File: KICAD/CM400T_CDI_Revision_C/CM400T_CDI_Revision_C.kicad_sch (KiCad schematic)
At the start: 41 parts, among them P1 Brown, P2 Green Coil, P3 Black w/ White, P4 Yellow Coil, P5 Blue, P6 White, P7 Light Blue, P8 Green Harness, P9 Pink

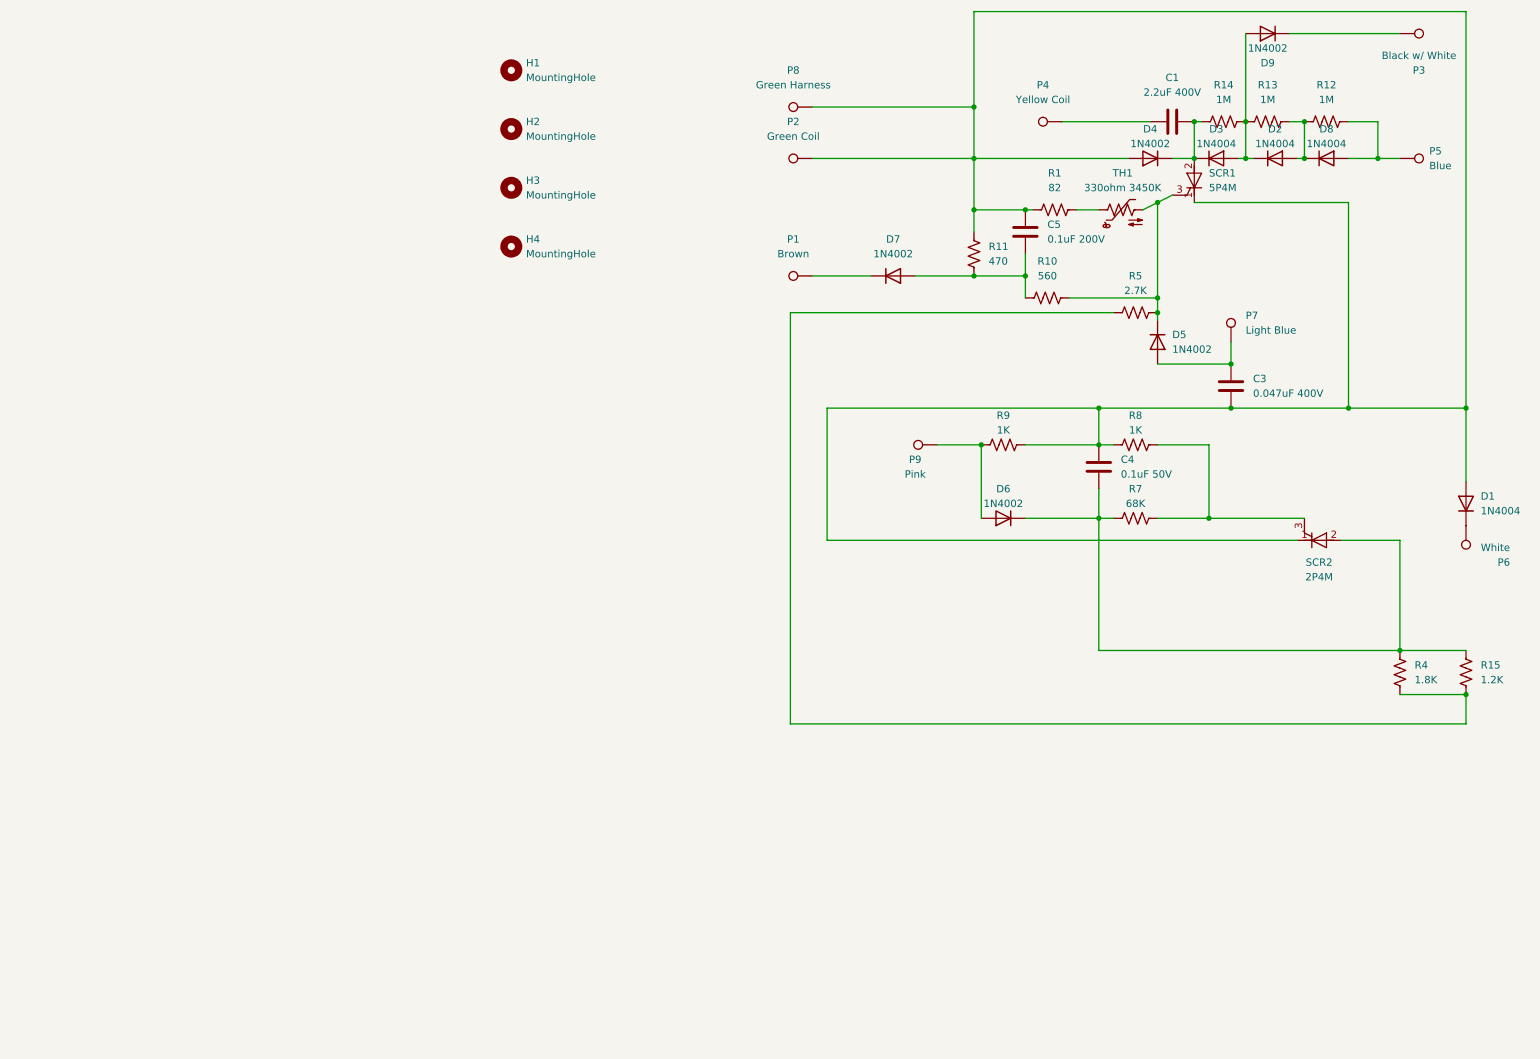
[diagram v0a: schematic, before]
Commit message: Redraw schematic to match structure of diagram from manual. No electrical / functional changes
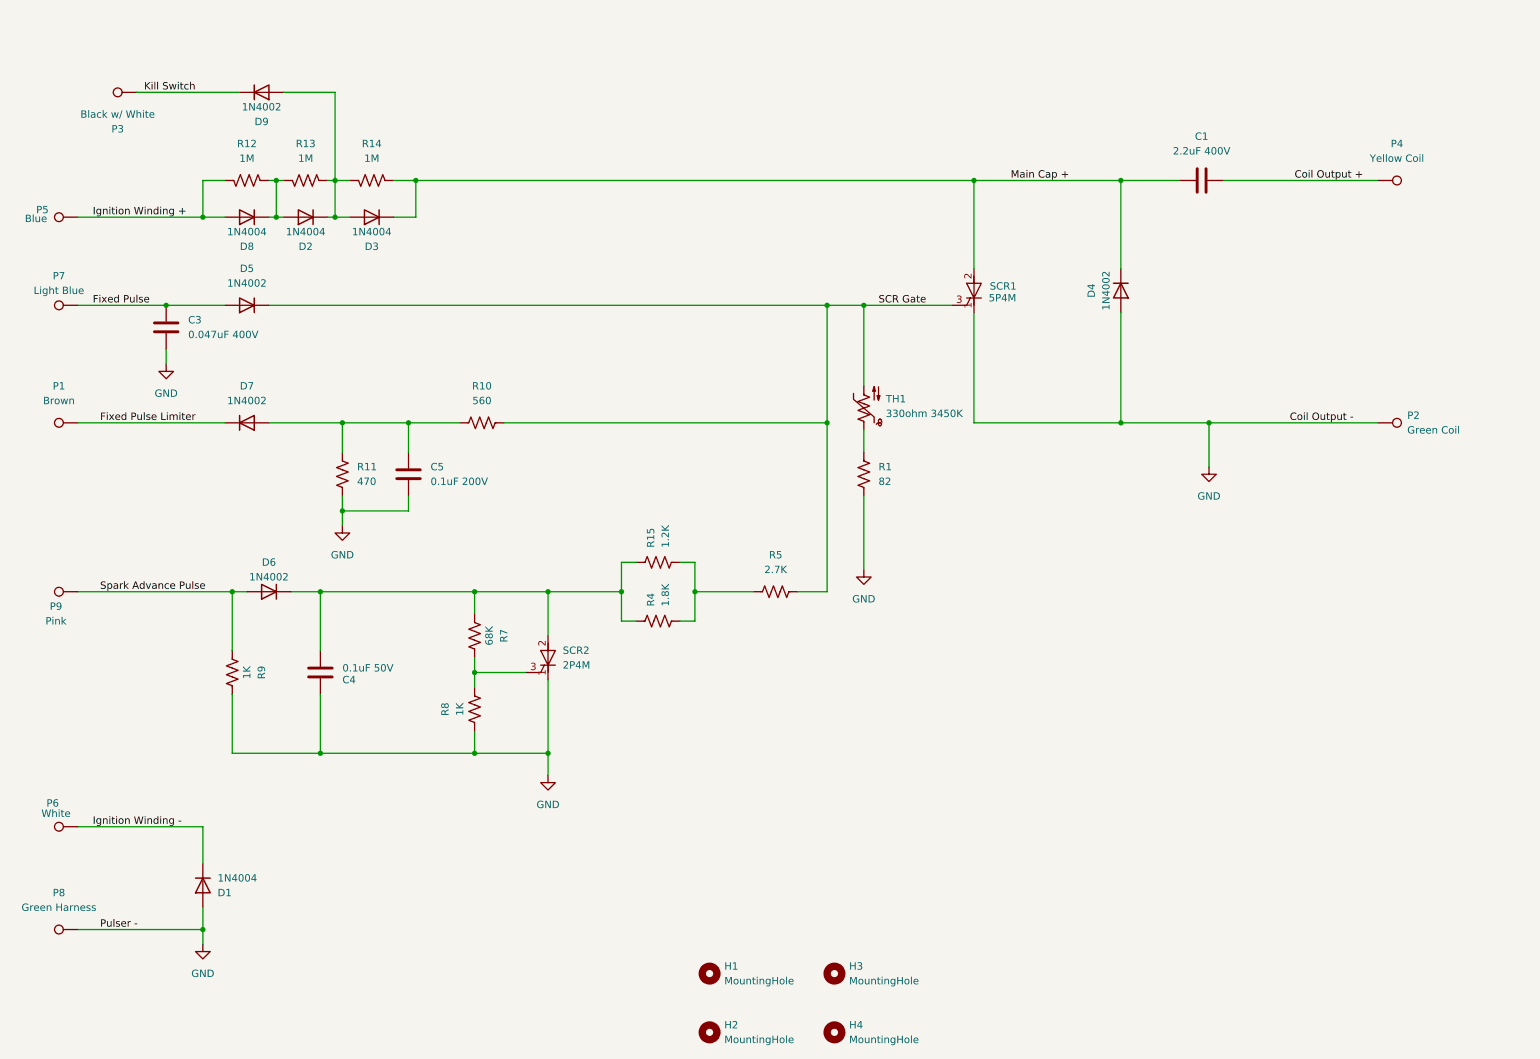
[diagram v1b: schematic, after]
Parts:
- C5: footprint Capacitor_THT:C_Axial_L3.8mm_D2.6mm_P12.50mm_Horizontal -> Capacitor_THT:C_Axial_L3.8mm_D2.6mm_P15.00mm_Horizontal
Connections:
- net Ignition Winding -: now reaches D1.1 (K), P6.1
- net GND: now reaches C3.2, C4.1, C5.2, D1.2 (A), D4.2 (A), P2.1, P8.1, R1.1, R11.1, R8.1, R9.2, SCR1.1 (K), SCR2.1 (K)
- net Main Cap +: now reaches C1.2, D3.1 (K), D4.1 (K), R14.1, SCR1.2 (A)
- net SCR Gate: now reaches D5.1 (K), R10.2, R5.2, SCR1.3 (G), TH1.2
- net Spark Advance Pulse: now reaches D6.2 (A), P9.1, R9.1
- net Fixed Pulse Limiter: now reaches D7.1 (K), P1.1
- net Coil Output +: now reaches C1.1, P4.1
- net Kill Switch: now reaches D9.1 (K), P3.1
- net Fixed Pulse: now reaches C3.1, D5.2 (A), P7.1
- net Ignition Winding +: now reaches D8.2 (A), P5.1, R12.1
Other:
- moved on the sheet: C1, C3, C4, C5, D1, D2, D3, D4, D5, D6, D7, D8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

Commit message: Add footprint file for 35mm capacitor to fix DRC violation
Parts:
- C1: footprint Capacitor_THT:C_Axial_L3.8mm_D2.6mm_P12.50mm_Horizontal -> footprints:C_Axial_L3.8mm_D2.6mm_P35.00mm_Horizontal
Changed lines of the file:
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@@
 			"3uvSlIUPRIG014WlBCxqh1z0imRm11nh1nI2SGSCdQ2FLKw0/CuDuYJWLdAgpF6PSaZSqStloVWV"
 			"M7FAfSczx+ysk+zxUmLAQs6Iv7J7K4HwlmyzErp9aQEjRO54VgIIVo4SWFD0wE6Lps9adrcBpIG7"
-			"iw3DcLlckOb/A3P5Xpd7T4mZAAAAAElFTkSuQmCC"
+			"iw3DcLlckOb/A3P5Xpd7T4mZAAAAAElFTkSuQmCCeIx0cAd7CAd5SIdwcAd6cAN2eIdwIIcZzBEO"
+			"7JAO4TAPbjAP4/AO8FAOMxDEHd4hHNghHcJhHmYwiTu8gzvQQzm0Azy8gzyEAzvM8BR2YAd7aAc3"
+			"aIdyaAc3gIdwkIdwYAd2KAd2+AV2eId3gIdfCIdxGIdymId5mIEs7vAO7uAO9cAO7DADYsihHOSh"
+			"HMyhHOShHNxhHMohHMSBHcphBtaQQznIQzmYQznIQzm4wziUQziIAzuUwy+8gzz8gjvUAzuwwwzH"
+			"aYdwWIdycIN0aAd4YId0GId0oIcZzlMP7gAP8lAO5JAO40AP4SAO7FAOMyAoHdzBHsJBHtIhHNyB"
+			"HtzgHOThHeoBHmYYUTiwQzqcgzvMUCR2YAd7aAc3YId3eAd4mFFM9JAP8FAOMx5qHsphHOghHd7B"
+			"HX4BHuShHMwhHfBhBlSFgzjMwzuwQz3QQzn8wjzkQzuIwzuww4zFCod5mId3GId0CAd6KAdymIFc"
+			"4xAO7MAO5VAO8zAjwdJBHuThF9jhHd4BHgAAAAB5IAAADQMAAGIeSCBDiAwZORkkkJFAxsjIaCJQ"
+			"CBQynhgZIUfIkFGkB16wQwEAAABNhCSHcylJE12X8zgP96gBx02ShnFKR1lTdRlIhGFalxhLdBUG"
+			"sTzXdVHTZVyG1WjR0ijSAlWPASGagylGJEEb1iwM8mAYRUmSJEULUU1fGFiZshwX9kCcBAAAAGZ1"
+			"bmN0aW9uX3R5cGVpbXBsaWNpdF9hcmdfZGVzY01vZHVsZU1EaXNQcmVjaXNlY29tcE9wdERlbm9y"
+			"bXNBcmVaZXJvQ29ycmVjdGx5Um91bmRlZERpdlNxcnRPcHREaXNhYmxlTWFkRW5hYmxlTm9TaWdu"
+			"ZWRaZXJvc0Zsb2F0Um91bmRpbmdNb2RlRmxvYXRDdnRJbnRSb3VuZGluZ01vZGVVbnNhZmVNYXRo"
+			"T3B0aW1pemF0aW9uc0Zpbml0ZU1hdGhPbmx5RmFzdFJlbGF4ZWRNYXRoRGFzaEdTcGVjaWZpZWRG"
+			"YXN0Q29tcGlsYXRpb25Vc2VTY3JhdGNoU3BhY2VQcml2YXRlTWVtb3J5UmVsYXhlZEJ1aWx0aW5z"
+			"U3ViZ3JvdXBJbmRlcGVuZGVudEZvcndhcmRQcm9ncmVzc1JlcXVpcmVkR3JlYXRlclRoYW4yR0JC"
+			"dWZmZXJSZXF1aXJlZEdyZWF0ZXJUaGFuNEdCQnVmZmVyUmVxdWlyZWRQdXNoQ29uc3RhbnRzRW5h"
+			"YmxlSGFzQnVmZmVyT2Zmc2V0QXJncmVwbGFjZUdsb2JhbE9mZnNldHNCeVplcm9mb3JjZVBpeGVs"
+			"U2hhZGVyU0lNRE1vZGVwaXhlbFNoYWRlckRvTg=="
 		)
 	)
@@
 			)
 		)
-		(property "Footprint" "Capacitor_THT:C_Axial_L3.8mm_D2.6mm_P12.50mm_Horizontal"
+		(property "Footprint" "footprints:C_Axial_L3.8mm_D2.6mm_P35.00mm_Horizontal"
 			(at 218.44 43.4848 0)
 			(effects

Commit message: Add ColorCode field to wire hole symbols so that code can be displayed on silkscreen instead of reference designator
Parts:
- P1: ColorCode (none) -> BR
- P2: ColorCode (none) -> GR
- P3: ColorCode (none) -> BW
- P4: ColorCode (none) -> Y
- P5: ColorCode (none) -> BL
- P6: ColorCode (none) -> WH
- P7: ColorCode (none) -> LB
- P8: ColorCode (none) -> GH
- P9: ColorCode (none) -> PI
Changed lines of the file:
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@@
 			"dWZmZXJSZXF1aXJlZEdyZWF0ZXJUaGFuNEdCQnVmZmVyUmVxdWlyZWRQdXNoQ29uc3RhbnRzRW5h"
 			"YmxlSGFzQnVmZmVyT2Zmc2V0QXJncmVwbGFjZUdsb2JhbE9mZnNldHNCeVplcm9mb3JjZVBpeGVs"
-			"U2hhZGVyU0lNRE1vZGVwaXhlbFNoYWRlckRvTg=="
+			"U2hhZGVyU0lNRE1vZGVwaXhlbFNoYWRlckRvTgAAAAAAAAAAAAAAAAAAAAAAAAAAAAAAAAAAAAAA"
+			"AAAAAAAAAAAAAAAAAAAAAAAAAAAAAAAAAAAAAAAAAAAAAAAAAAAAAAAAAAAAAAAAAAAAAAAAAAAA"
+			"AAAAAAAAAAAAAAAAAAAAAAAAAAAAAAAAAAAAAAAAAAAAAAAAAAAAAAAAAAAAAAAAAAAAAAAAAAAA"
+			"AAAAAAAAAAAAAAAAAAAAAAAAAAAAAAAAAAAAAAAAAAAAAAAAAAAAAAAAAAAAAAAAAAAAAAAAAAAA"
+			"AAAAAAAAAAAAAAAAAAAAAAAAAAAAAAAAAAAAAAAAAAAAAAAAAAAAAAAAAAAAAAAAAAAAAAAAAAAA"
+			"AAAAAAAAAAAAAAAAAAAAAAAAAAAAAAAAAAAAAAAAAAAAAAAAAAAAAAAAAAAAAAAAAAAAAAAAAAAA"
+			"AAAAAAAAAAAAAAAAAAAAAAAAAAAAAAAAAAAAAAAAAAAAAAAAAAAAAAAAAAAAAAAAAAAAAAAAAAAA"
+			"AAAAAAAAAAAAAAAAAAAAAAAAAAAAAAAAAAAAAAAAAAAAAAAAAAAAAAAAAAAAAAAAAAAAAAAAAAAA"
+			"AAAAAAAAAAAAAAAAAAAAAAAAAAAAAAAAAAAAAAAAAAAAAAAAAAAAAAAAAAAAAAAAAAAAAAAAAAAA"
+			"AAAAAAAAAAAAAAAAAAAAAAAAAAAAAAAAAAAAAAAAAAAAAAAAAAAAAAAAAAAAAAAAAAAAAAAAAAAA"
+			"AAAAAAAAAAAAAAAAAAAAAAAAAAAAAAAAAAAAAAAAAAAAAAAAAAAAAAAAAAAAAAAAAAAAAAAAAAAA"
+			"AAAAAAAAAAAAAAAAAAAAAAAAAAAAAAAAAAAAAAAAAAAAAAAAAAAAAAAAAAAAAAAAAAAAAAAAAAAA"
+			"AAAAAAAAAAAAAAAAAAAAAAAAAAAAAAAAAAAAAAAAAAAAAAAAAAAAAAAAAAAAAAAAAAAAAAAAAAAA"
+			"AAAAAAAAAAAAAAAAAAAAAAAAAAAAAAAAAAAAAAAAAAAAAAAAAAAAAAAAAAAAAAAAAAAAAAAAAAAA"
+			"AAAAAAAAAAAAAAAAAAAAAAAAAAAAAAAAAAAAAAAAAAAAAAAAAAAAAAAAAAAAAAAAAAAAAAAAAAAA"
+			"AAAAAAAAAAAAAAAAAAAAAAAAAAAAAAAAAAAAAAAAAAAAAAAAAAAAAAAAAAAAAAAAAAAAAAAAAAAA"
+			"AAAAAAAAAAAAAAAAAAAAAAAAAAAAAAAAAAAAAAAAAAAAAAAAAAAAAAAAAAAAAAAAAAAAAAAAAAAA"
+			"AAAAAAAAAAAAAAAAAAAAAAAAAAAAAAAAAAAAAAAAAAAAAAAAAAAAAAAAAAAAAAAAAAAAAAAAAAAA"
+			"AAAAAAAAAAAAAAAAAAAAAAAAAAAAAAAAAAAAAAAAAAAAAAAAAAAAAAAAAAAAAAAAAAAAAAAAAAAA"
+			"AAAAAAAAAAAAAAAAAAAAAAAAAAAAAAAAAAAAAAAAAAAAAAAAAAAAAAAAAAAAAAAAAAAAAAAAAAAA"
+			"AAAAAAAAAAAAAAAAAAAAAAAAAAAAAAAAAAAAAAAAAAAAAAAAAAAAAAAAAAAAAAAAAAAAAAAAAAAA"
+			"AAAAAAAAAAAAAAAAAAAAAAAAAAAAAAAAAAAAAAAAAAAAAAAAAAAAAAAAAAAAAAAAAAAAAAAAAAAA"
+			"AAAAAAAAAAAAAAAAAAAAAAAAAAAAAAAAAAAAAAAAAAAAAAAAAAAAAAAAAAAAAAAAAAAAAAAAAAAA"
+			"AAAAAAAAAAAAAAAAAAAAAAAAAAAAAAAAAAAAAAAAAAAAAAAAAAAAAAAAAAAAAAAAAAAAAAAAAAAA"
+			"AAAAAAAAAAAAAAAAAAAAAAAAAAAAAAAAAAAAAAAAAAAAAAAAAAAAAAAAAAAAAAAAAAAAAAAAAAAA"
+			"AAAAAAAAAAAAAAAAAAAAAAAAAAAAAAAAAAAAAAAAAAAAAAAAAAAAAAAAAAAAAAAAAAAAAAAAAAAA"
+			"AAAAAAAAAAAAAAAAAAAAAAAAAAAAAAAAAAAAAAAAAAAAAAAAAAAAAAAAAAAAAAAAAAAAAAAAAAAA"
+			"AAAAAAAAAAAAAAAAAAAAAAAAAAAAAAAAAAAAAAAAAAAAAAAAAAAAAAAAAAAAAAAAAAAAAAAAAAAA"
+			"AAAAAAAAAAAAAAAAAAAAAAAAAAAAAAAAAAAAAAAAAAAAAAAAAAAAAAAAAAAAAAAAAAAAAAAAAAAA"
+			"AAAAAAAAAAAAAAAAAAAAAAAAAAAAAAAAAAAAAAAAAAAAAAAAAAAAAAAAAAAAAAAAAAAAAAAAAAAA"
+			"AAAAAAAAAAAAAAAAAAAAAAAAAAAAAAAAAAAAAAAAAAAAAAAAAAAAAAAAAAAAAAAAAAAAAAAAAAAA"
+			"AAAAAAAAAAAAAAAAAAAAAAAAAAAAAAAAAAAAAAAAAAAAAAAAAAAAAAAAAAAAAAAAAAAAAAAAAAAA"
+			"AAAAAAAAAAAAAAAAAAAAAAAAAAAAAAAAAAAAAAAAAAAAAAAAAAAAAAAAAAAAAAAAAAAAAAAAAAAA"
+			"AAAAAAAAAAAAAAAAAAAAAAAAAAAAAAAAAAAAAAAAAAAAAAAAAAAAAAAAAAAAAAAAAAAAAAAAAAAA"
+			"AAAAAAAAAAAAAAAAAAAAAAAAAAAAAAAAAAAAAAAAAAAAAAAAAAAAAAAAAAAAAAAAAAAAAAAAAAAA"
+			"AAAAAAAAAAAAAAAAAAAAAAAAAAAAAAAAAAAAAAAAAAAAAAAAAAAAAAAAAAAAAAAAAAAAAAAAAAAA"
+			"AAAAAAAAAAAAAAAAAAAAAAAAAAAAAAAAAAAAAA=="
 		)
 	)
@@
 		(on_board yes)
 		(dnp no)
-		(fields_autoplaced yes)
 		(property "Reference" "P1"
 			(at 24.638 80.01 90)
@@
 			)
 		)
+		(property "ColorCode" "BR"
+			(at 24.638 89.154 90)
+			(effects
+				(font
+					(size 1.27 1.27)
+				)
+			)
+		)
 		(pin "1"
 		)
@@
 		(on_board yes)
 		(dnp no)
-		(fields_autoplaced yes)
 		(property "Reference" "P8"
 			(at 24.638 167.64 90)
@@
 			)
 		)
+		(property "ColorCode" "GH"
+			(at 24.638 177.038 90)
+			(effects
+				(font
+					(size 1.27 1.27)
+				)
+			)
+		)
 		(pin "1"
 		)
@@
 		(on_board yes)
 		(dnp no)
-		(fields_autoplaced yes)
 		(property "Reference" "P3"
 			(at 34.798 35.56 90)
@@
 			)
 		)
+		(property "ColorCode" "BW"
+			(at 34.544 25.908 90)
+			(effects
+				(font
+					(size 1.27 1.27)
+				)
+			)
+		)
 		(pin "1"
 		)
@@
 		(on_board yes)
 		(dnp no)
-		(fields_autoplaced yes)
 		(property "Reference" "P7"
 			(at 24.638 60.96 90)
@@
 			)
 		)
+		(property "ColorCode" "LB"
+			(at 24.638 68.834 90)
+			(effects
+				(font
+					(size 1.27 1.27)
+				)
+			)
+		)
 		(pin "1"
 		)
@@
 		(on_board yes)
 		(dnp no)
-		(fields_autoplaced yes)
 		(property "Reference" "P2"
 			(at 257.81 85.0899 90)
@@
 			)
 		)
+		(property "ColorCode" "GR"
+			(at 255.778 82.55 90)
+			(effects
+				(font
+					(size 1.27 1.27)
+				)
+			)
+		)
 		(pin "1"
 		)
@@
 			)
 		)
+		(property "ColorCode" "PI"
+			(at 24.638 112.268 90)
+			(effects
+				(font
+					(size 1.27 1.27)
+				)
+			)
+		)
 		(pin "1"
 		)
@@
 		(on_board yes)
 		(dnp no)
-		(fields_autoplaced yes)
 		(property "Reference" "P4"
 			(at 256.032 38.1 90)
@@
 			)
 		)
+		(property "ColorCode" "Y"
+			(at 256.032 47.498 90)
+			(effects
+				(font
+					(size 1.27 1.27)
+				)
+			)
+		)
 		(pin "1"
 		)
@@
 			)
 		)
+		(property "ColorCode" "WH"
+			(at 24.384 158.75 90)
+			(effects
+				(font
+					(size 1.27 1.27)
+				)
+			)
+		)
 		(pin "1"
 		)
@@
 			(effects
 				(font
+					(size 1.27 1.27)
+				)
+			)
+		)
+		(property "ColorCode" "BL"
+			(at 24.638 47.244 90)
+			(effects
+				(font
